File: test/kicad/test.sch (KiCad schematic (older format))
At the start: 2 parts

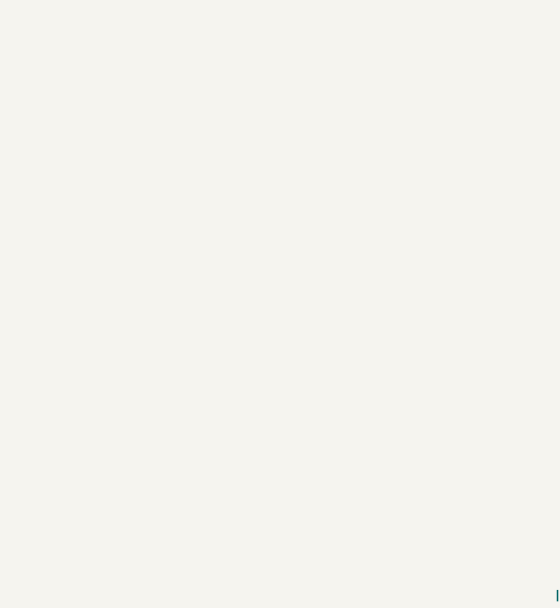
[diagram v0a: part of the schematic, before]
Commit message: Parse the component library.
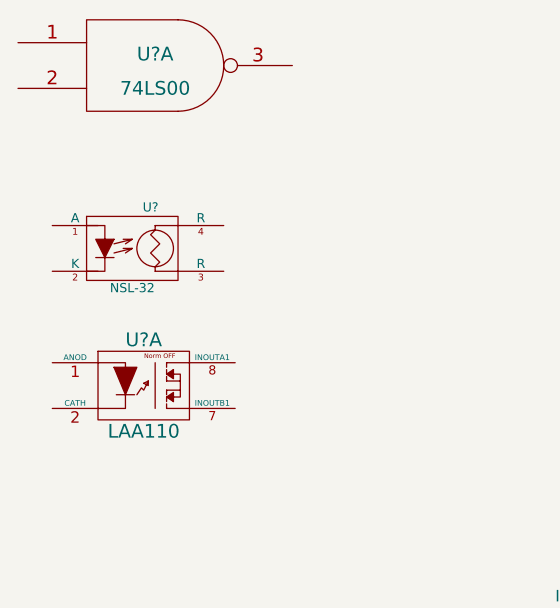
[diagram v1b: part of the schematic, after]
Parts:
- added U?: 74LS00, symbol 74LS00
- added U?: NSL-32, symbol NSL-32
- added U?: LAA110, symbol LAA110
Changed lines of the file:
@@
-EESchema Schematic File Version 2  date Fri 07 Oct 2011 11:59:12 AM EDT
+EESchema Schematic File Version 2  date Sun 11 Dec 2011 09:38:15 PM PST
 LIBS:power
 LIBS:device
@@
 LIBS:contrib
 LIBS:valves
-EELAYER 24  0
+LIBS:test-cache
+EELAYER 25  0
 EELAYER END
 $Descr A4 11700 8267
+encoding utf-8
 Sheet 1 1
 Title ""
-Date "7 oct 2011"
+Date "12 dec 2011"
 Rev ""
 Comp ""
@@
 Comment4 ""
 $EndDescr
+$Comp
+L LAA110 U?
+U 1 1 4EE59331
+P 1650 2650
+F 0 "U?" H 1650 2850 60  0000 C CNN
+F 1 "LAA110" H 1650 2450 60  0000 C CNN
+	1    1650 2650
+	1    0    0    -1
+$EndComp
+$Comp
+L NSL-32 U?
+U 1 1 4EE58F9A
+P 1600 2050
+F 0 "U?" H 1680 2230 40  0000 C CNN
+F 1 "NSL-32" H 1600 1877 40  0000 C CNN
+	1    1600 2050
+	1    0    0    -1
+$EndComp
+$Comp
+L 74LS00 U?
+U 1 1 4EE57ED5
+P 1700 1250
+F 0 "U?" H 1700 1300 60  0000 C CNN
+F 1 "74LS00" H 1700 1150 60  0000 C CNN
+	1    1700 1250
+	1    0    0    -1
+$EndComp
 Wire Wire Line
 	5150 4050 6900 4050
